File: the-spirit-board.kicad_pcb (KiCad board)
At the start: 2 copper layers, 1 part, among them IC1 ESP32-C6-WROOM-1-N8

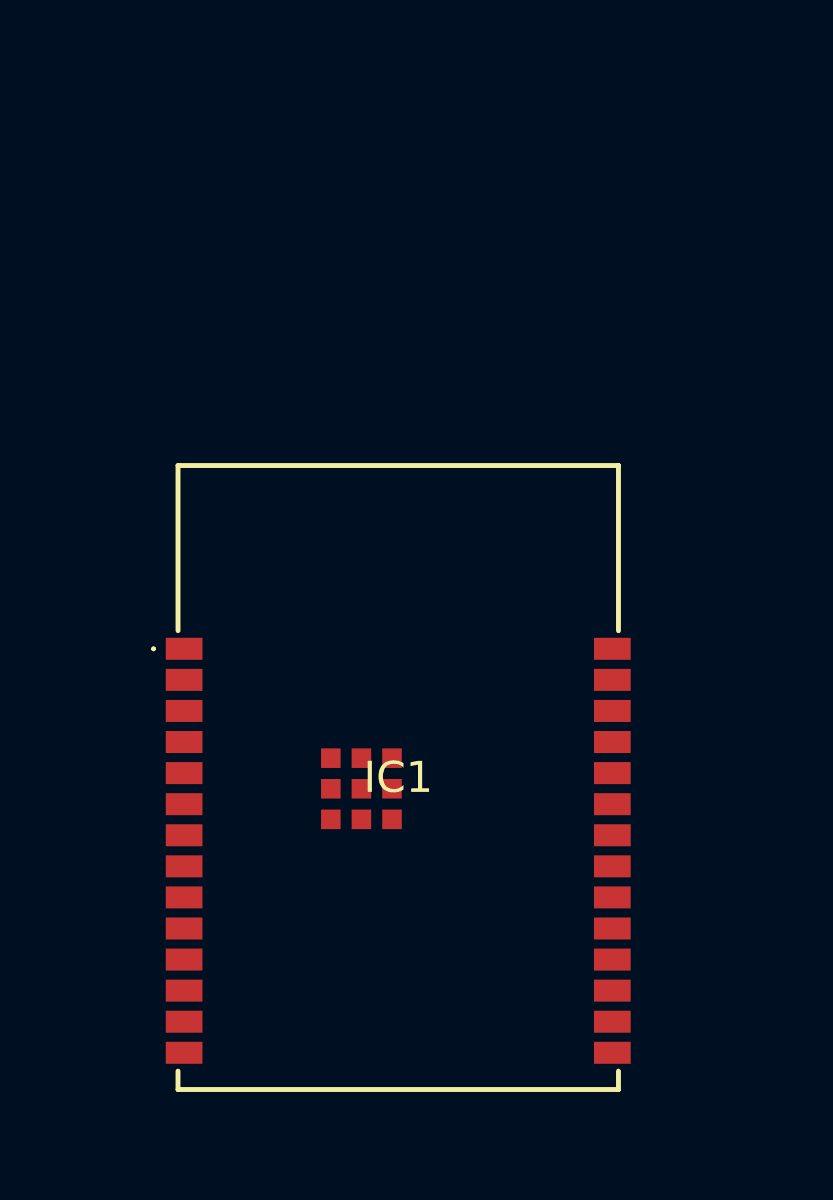
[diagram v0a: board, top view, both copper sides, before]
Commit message: Add power supply and momentary switch for enable
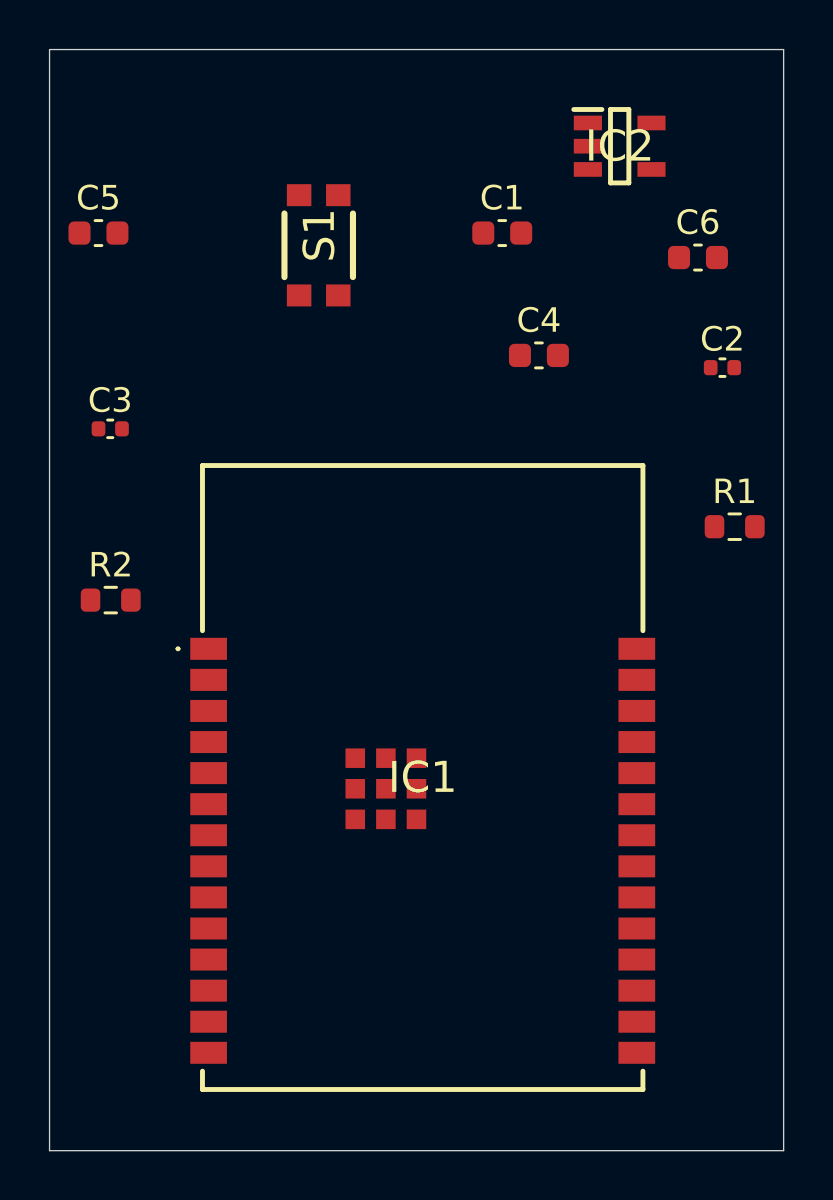
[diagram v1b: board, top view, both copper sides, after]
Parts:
- added C1: 1uF, Capacitor_SMD:C_0603_1608Metric, F.Cu at (158.5, 77.5)
- added C2: 0.1uF, Capacitor_SMD:C_0402_1005Metric, F.Cu at (167.5, 83.0)
- added C3: 0.1uF, Capacitor_SMD:C_0402_1005Metric, F.Cu at (142.5, 85.5)
- added C4: 10uF, Capacitor_SMD:C_0603_1608Metric, F.Cu at (160.0, 82.5)
- added C5: 10uF, Capacitor_SMD:C_0603_1608Metric, F.Cu at (142.0, 77.5)
- added C6: 10uF, Capacitor_SMD:C_0603_1608Metric, F.Cu at (166.5, 78.5)
- added IC2: AP2112K-3.3TRG1, TheSPIRITBoard:SOT95P285X140-5N, F.Cu at (163.3, 74.0)
- added R1: 5.1k, Resistor_SMD:R_0603_1608Metric, F.Cu at (168.0, 89.5)
- added R2: 100k, Resistor_SMD:R_0603_1608Metric, F.Cu at (142.5, 92.5)
- added S1: KMR211G_LFS, TheSPIRITBoard:KMR_2, F.Cu at (151.0, 78.0)
- moved IC1 1.00 mm to (155.2, 99.8)
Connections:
- IC1 pad 1: unconnected-(IC1-GND_1-Pad1) -> GND
- IC1 pad 10: unconnected-(IC1-IO8-Pad10) -> /IO8
- IC1 pad 11: unconnected-(IC1-IO10-Pad11) -> /IO10
- IC1 pad 12: unconnected-(IC1-IO11-Pad12) -> /IO11
- IC1 pad 13: unconnected-(IC1-IO12-Pad13) -> /IO12
- IC1 pad 14: unconnected-(IC1-IO13-Pad14) -> /IO13
- IC1 pad 15: unconnected-(IC1-IO9-Pad15) -> /IO9
- IC1 pad 16: unconnected-(IC1-IO18-Pad16) -> /IO18
- IC1 pad 17: unconnected-(IC1-IO19-Pad17) -> /IO19
- IC1 pad 18: unconnected-(IC1-IO20-Pad18) -> /IO20
- IC1 pad 19: unconnected-(IC1-IO21-Pad19) -> /IO21
- IC1 pad 2: unconnected-(IC1-3V3-Pad2) -> +3.3V
- IC1 pad 20: unconnected-(IC1-IO22-Pad20) -> /IO22
- IC1 pad 21: unconnected-(IC1-IO23-Pad21) -> /IO23
- IC1 pad 23: unconnected-(IC1-IO15-Pad23) -> /IO15
- IC1 pad 24: unconnected-(IC1-RXD0-Pad24) -> /RXD0
- IC1 pad 25: unconnected-(IC1-TXD0-Pad25) -> /TXD0
- IC1 pad 26: unconnected-(IC1-IO3-Pad26) -> /IO3
- IC1 pad 27: unconnected-(IC1-IO2-Pad27) -> /IO20
- IC1 pad 28: unconnected-(IC1-GND_2-Pad28) -> GND
- IC1 pad 29: unconnected-(IC1-GND_3-Pad29) -> GND
- IC1 pad 3: unconnected-(IC1-EN-Pad3) -> /EN
- IC1 pad 30: unconnected-(IC1-GND_4-Pad30) -> GND
- IC1 pad 31: unconnected-(IC1-GND_5-Pad31) -> GND
- IC1 pad 32: unconnected-(IC1-GND_6-Pad32) -> GND
- IC1 pad 33: unconnected-(IC1-GND_7-Pad33) -> GND
- IC1 pad 34: unconnected-(IC1-GND_8-Pad34) -> GND
- IC1 pad 35: unconnected-(IC1-GND_9-Pad35) -> GND
- IC1 pad 36: unconnected-(IC1-GND_10-Pad36) -> GND
- IC1 pad 37: unconnected-(IC1-GND_11-Pad37) -> GND
- IC1 pad 4: unconnected-(IC1-IO4-Pad4) -> /IO4
- IC1 pad 5: unconnected-(IC1-IO5-Pad5) -> /IO5
- IC1 pad 6: unconnected-(IC1-IO6-Pad6) -> /IO6
- IC1 pad 7: unconnected-(IC1-IO7-Pad7) -> /IO7
- IC1 pad 8: unconnected-(IC1-IO0-Pad8) -> /IO0
- IC1 pad 9: unconnected-(IC1-IO1-Pad9) -> /IO1
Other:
- board outline added: 30 x 45 mm

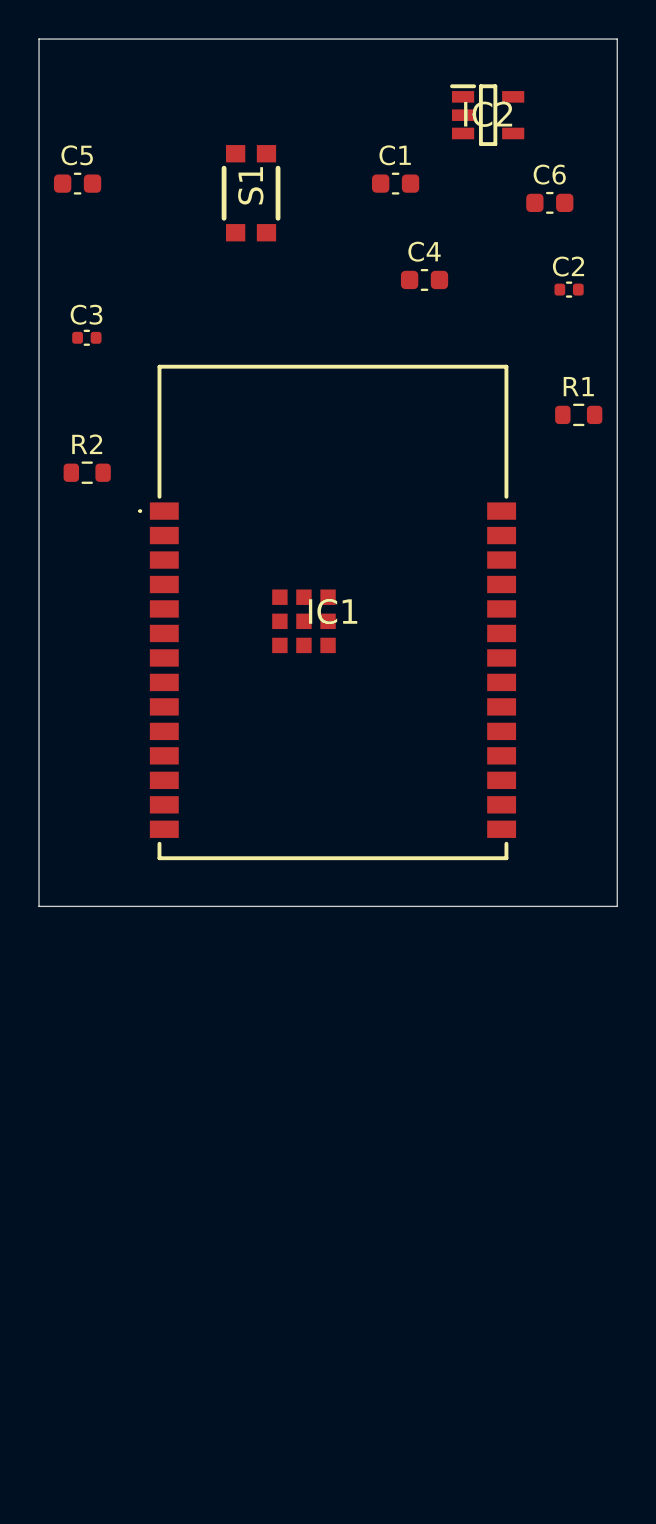
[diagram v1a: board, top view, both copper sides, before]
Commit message: Add the footprint for the Furby and do initial connections
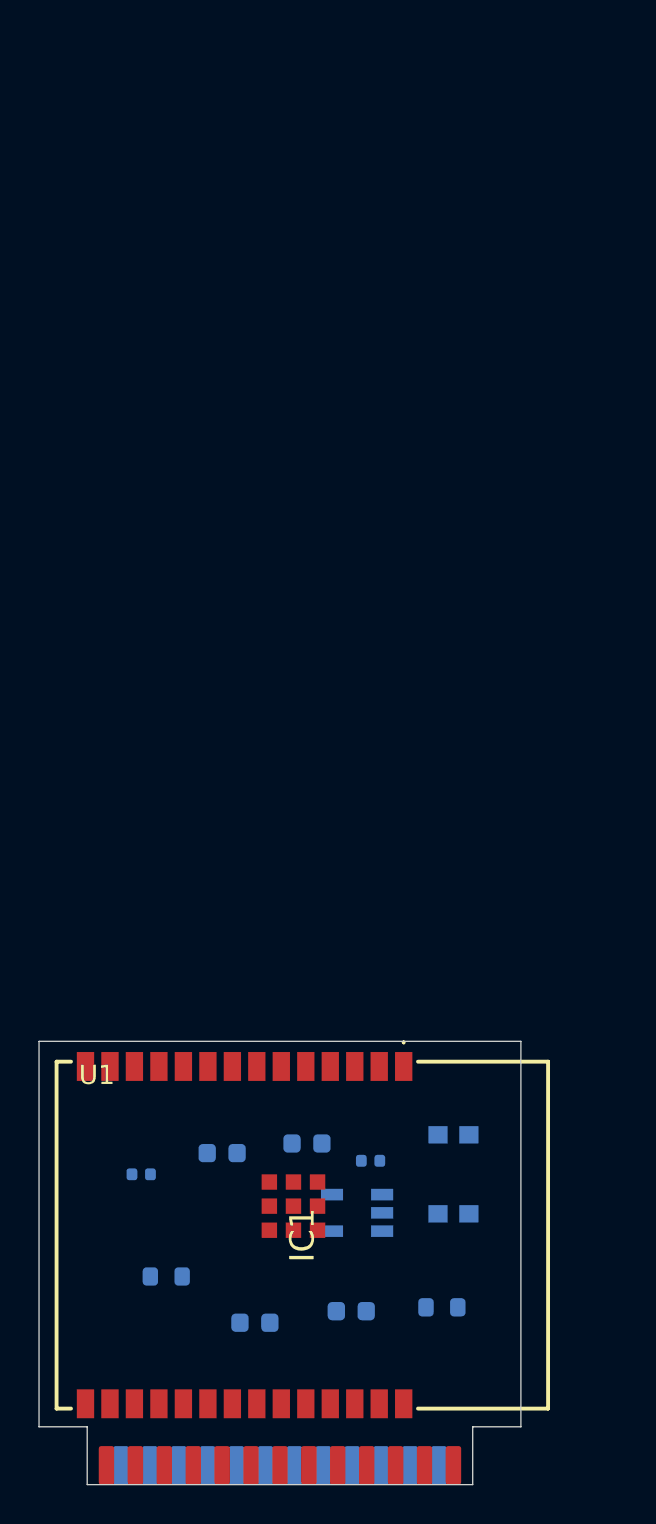
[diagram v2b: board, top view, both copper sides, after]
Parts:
- added U1: ~, TheSPIRITBoard:FURBY, F.Cu at (140.0, 122.0)
- C1, C2, C3, C4, C5, C6, IC2, R1, R2, S1: moved to B.Cu
- moved C6 60.1 mm to (151.2, 136.6), turned to 180 degrees
- moved IC2 57.4 mm to (156.5, 130.9), turned to 180 degrees
- moved C4 53.6 mm to (156.2, 136.0), turned to 180 degrees
- moved S1 52.0 mm to (161.5, 128.9)
- moved C5 50.9 mm to (149.5, 127.8), turned to 180 degrees
- moved C1 50.0 mm to (153.9, 127.3), turned to 180 degrees
- moved R1 46.8 mm to (160.9, 135.8), turned to 180 degrees
- moved C2 46.4 mm to (157.2, 128.2), turned to 180 degrees
- moved C3 43.5 mm to (145.3, 128.9), turned to 180 degrees
- moved R2 41.9 mm to (146.6, 134.2), turned to 180 degrees
- moved IC1 32.3 mm to (153.7, 132.1), turned to -90 degrees
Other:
- board size 30 x 45 mm -> 25 x 23 mm

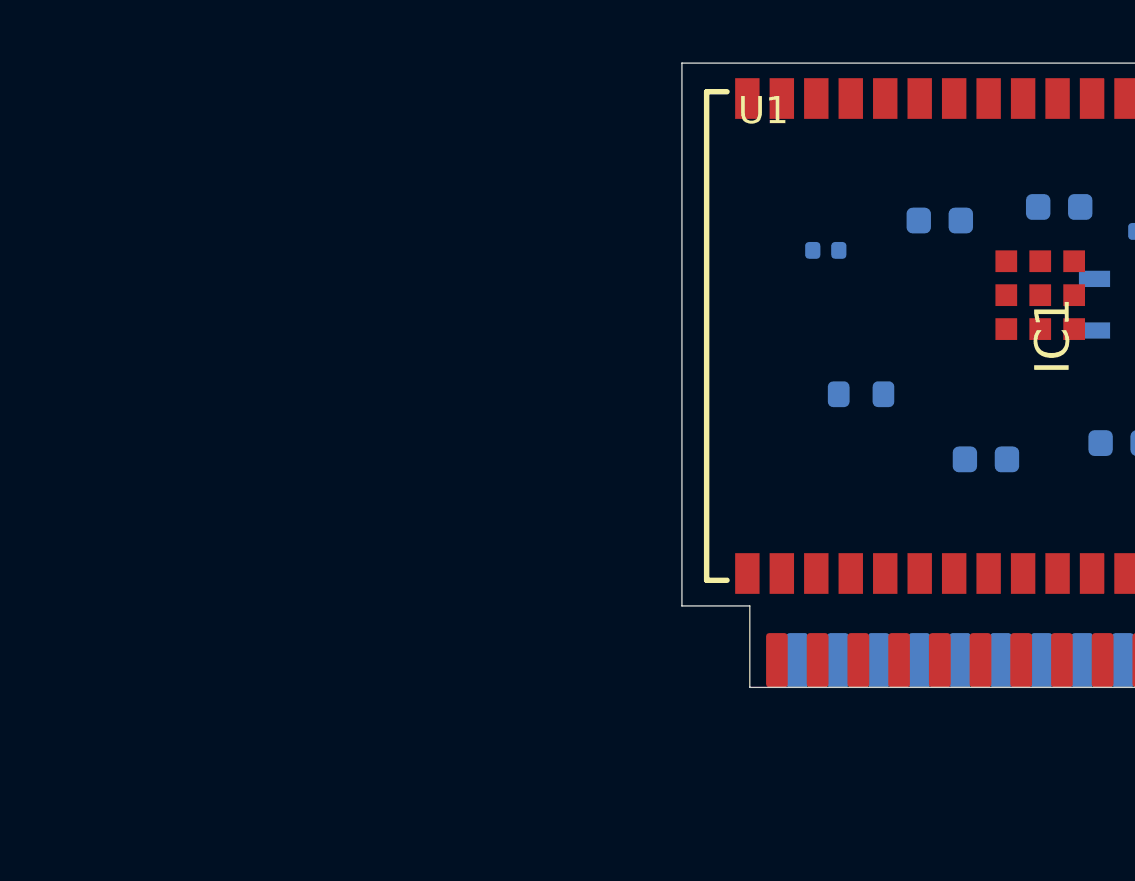
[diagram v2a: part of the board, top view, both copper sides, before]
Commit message: Completed connection between the Furby and the ESP32-C6
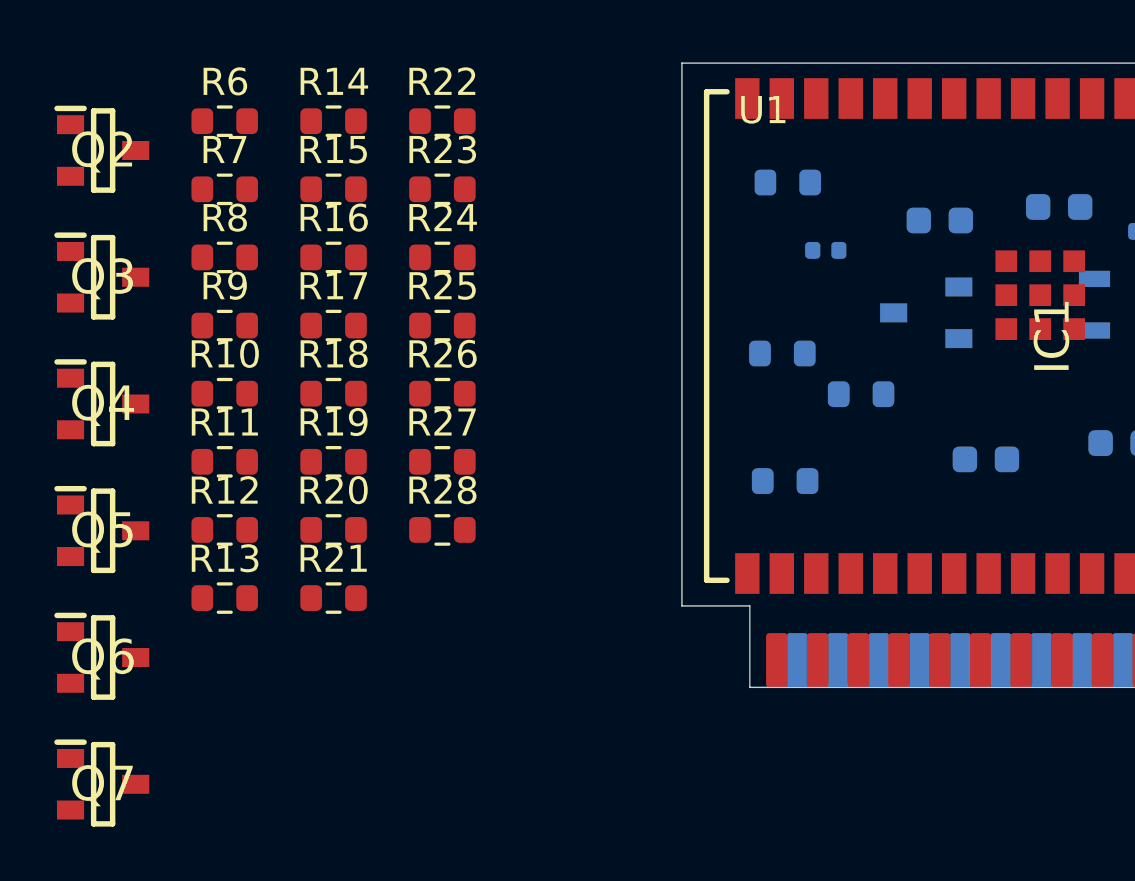
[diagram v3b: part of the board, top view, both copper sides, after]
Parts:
- added Q1: BSS138, TheSPIRITBoard:SOT95P240X120-3N, B.Cu at (149.0, 131.2)
- added Q2: BSS138, TheSPIRITBoard:SOT95P240X120-3N, F.Cu at (118.7, 125.2)
- added Q3: BSS138, TheSPIRITBoard:SOT95P240X120-3N, F.Cu at (118.7, 129.9)
- added Q4: BSS138, TheSPIRITBoard:SOT95P240X120-3N, F.Cu at (118.7, 134.6)
- added Q5: BSS138, TheSPIRITBoard:SOT95P240X120-3N, F.Cu at (118.7, 139.2)
- added Q6: BSS138, TheSPIRITBoard:SOT95P240X120-3N, F.Cu at (118.7, 143.9)
- added Q7: BSS138, TheSPIRITBoard:SOT95P240X120-3N, F.Cu at (118.7, 148.6)
- added R10: 10k, Resistor_SMD:R_0603_1608Metric, F.Cu at (123.2, 134.2)
- added R11: 10k, Resistor_SMD:R_0603_1608Metric, F.Cu at (123.2, 136.7)
- added R12: 19k, Resistor_SMD:R_0603_1608Metric, F.Cu at (123.2, 139.2)
- added R13: 31k, Resistor_SMD:R_0603_1608Metric, F.Cu at (123.2, 141.7)
- added R14: 10k, Resistor_SMD:R_0603_1608Metric, F.Cu at (127.2, 124.1)
- added R15: 10k, Resistor_SMD:R_0603_1608Metric, F.Cu at (127.2, 126.7)
- added R16: 10k, Resistor_SMD:R_0603_1608Metric, F.Cu at (127.2, 129.2)
- added R17: 10k, Resistor_SMD:R_0603_1608Metric, F.Cu at (127.2, 131.7)
- added R18: 10k, Resistor_SMD:R_0603_1608Metric, F.Cu at (127.2, 134.2)
- added R19: 10k, Resistor_SMD:R_0603_1608Metric, F.Cu at (127.2, 136.7)
- added R20: 10k, Resistor_SMD:R_0603_1608Metric, F.Cu at (127.2, 139.2)
- added R21: 10k, Resistor_SMD:R_0603_1608Metric, F.Cu at (127.2, 141.7)
- added R22: 4.7k, Resistor_SMD:R_0603_1608Metric, F.Cu at (131.2, 124.1)
- added R23: 4.7k, Resistor_SMD:R_0603_1608Metric, F.Cu at (131.2, 126.7)
- added R24: 4.7k, Resistor_SMD:R_0603_1608Metric, F.Cu at (131.2, 129.2)
- added R25: 3.8k, Resistor_SMD:R_0603_1608Metric, F.Cu at (131.2, 131.7)
- added R26: 6.2k, Resistor_SMD:R_0603_1608Metric, F.Cu at (131.2, 134.2)
- added R27: 10k, Resistor_SMD:R_0603_1608Metric, F.Cu at (131.2, 136.7)
- added R28: 10k, Resistor_SMD:R_0603_1608Metric, F.Cu at (131.2, 139.2)
- added R3: 4.7k, Resistor_SMD:R_0603_1608Metric, B.Cu at (143.9, 126.4)
- added R4: 10k, Resistor_SMD:R_0603_1608Metric, B.Cu at (143.8, 137.4)
- added R5: 2.2k, Resistor_SMD:R_0603_1608Metric, B.Cu at (143.7, 132.7)
- added R6: 3.8k, Resistor_SMD:R_0603_1608Metric, F.Cu at (123.2, 124.1)
- added R7: 6.2k, Resistor_SMD:R_0603_1608Metric, F.Cu at (123.2, 126.7)
- added R8: 4.7k, Resistor_SMD:R_0603_1608Metric, F.Cu at (123.2, 129.2)
- added R9: 4.7k, Resistor_SMD:R_0603_1608Metric, F.Cu at (123.2, 131.7)
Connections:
- IC1 pad 27: /IO20 -> /IO2
- U1 pad 1: unconnected-(U1-SC1-Pad1) -> //INIT
- U1 pad 10: unconnected-(U1-TILT-Pad10) -> /TILT
- U1 pad 12: unconnected-(U1-SC2-Pad12) -> //CTS
- U1 pad 14: unconnected-(U1-SC3-Pad14) -> //RTS_(SDI)
- U1 pad 15: unconnected-(U1-SC4-Pad15) -> /D0
- U1 pad 16: unconnected-(U1-SC5-Pad16) -> /D1
- U1 pad 17: unconnected-(U1-SC6-Pad17) -> /D2_(SDO)
- U1 pad 18: unconnected-(U1-SC7-Pad18) -> /D3_(SCLK)
- U1 pad 2: unconnected-(U1-/FEED-Pad2) -> /IO15
- U1 pad 20: unconnected-(U1-/TUMMY-Pad20) -> /IO20
- U1 pad 21: unconnected-(U1-/BACK-Pad21) -> /IO21
- U1 pad 22: unconnected-(U1-GEAR_ROT-Pad22) -> /GEAR_ROT
- U1 pad 23: unconnected-(U1-/CAM_HOME-Pad23) -> /IO11
- U1 pad 24: unconnected-(U1-GND-Pad24) -> GND
- U1 pad 25: unconnected-(U1-+5.31V-Pad25) -> +5.31V
- U1 pad 3: unconnected-(U1-M_REVERSE-Pad3) -> /IO8
- U1 pad 4: unconnected-(U1-M_FORWARD-Pad4) -> /IO7
- U1 pad 5: unconnected-(U1-GEAR_LED-Pad5) -> /GEAR_LED
- U1 pad 6: unconnected-(U1-/POWER_DOWN-Pad6) -> /GEAR_LED
- U1 pad 8: unconnected-(U1-LIGHT-Pad8) -> /LIGHT
- U1 pad 9: unconnected-(U1-UPSIDE_DOWN-Pad9) -> /IO22
